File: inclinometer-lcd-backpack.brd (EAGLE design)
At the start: 78.7 x 25.4 mm, 13 parts, among them IC1 ATmega328-DIP-Prgrammed, Q1 2N3904, U1 LCD-16X2NOHOLES, Y1 16MHz

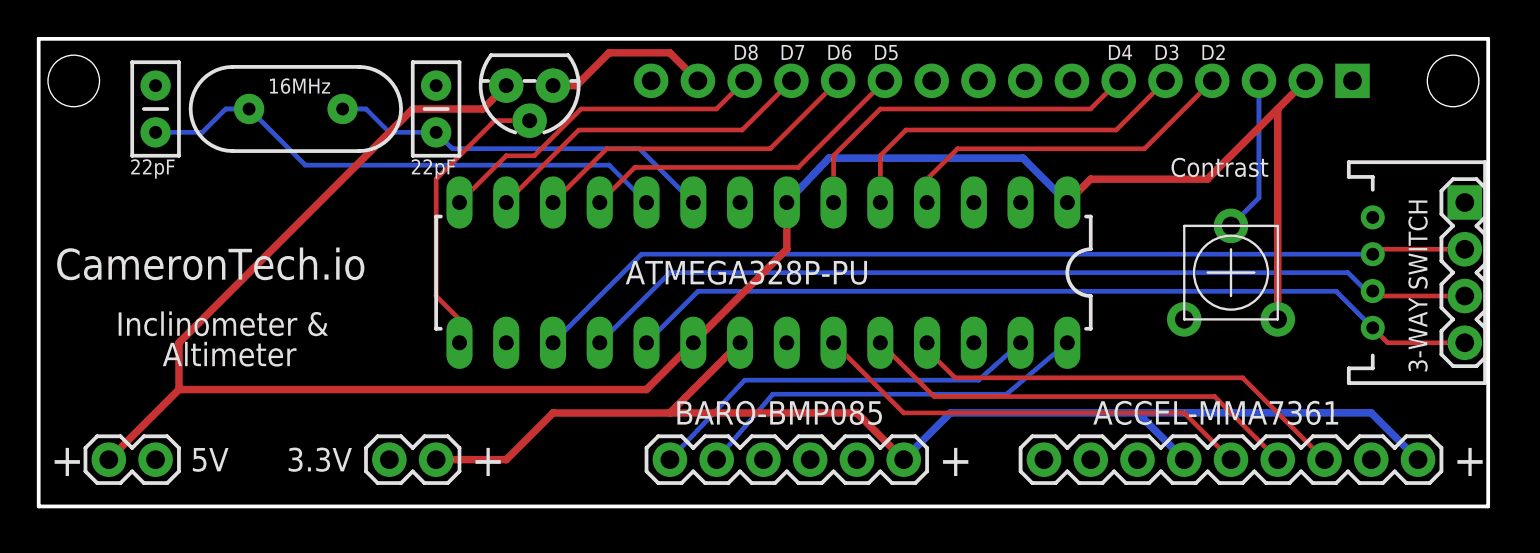
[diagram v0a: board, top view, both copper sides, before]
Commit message: Switches to 10DOF board from Sunkee
http://www.amazon.com/gp/product/B00CD239UG/ref=oh_details_o01_s00_i00?ie=UTF8&psc=1
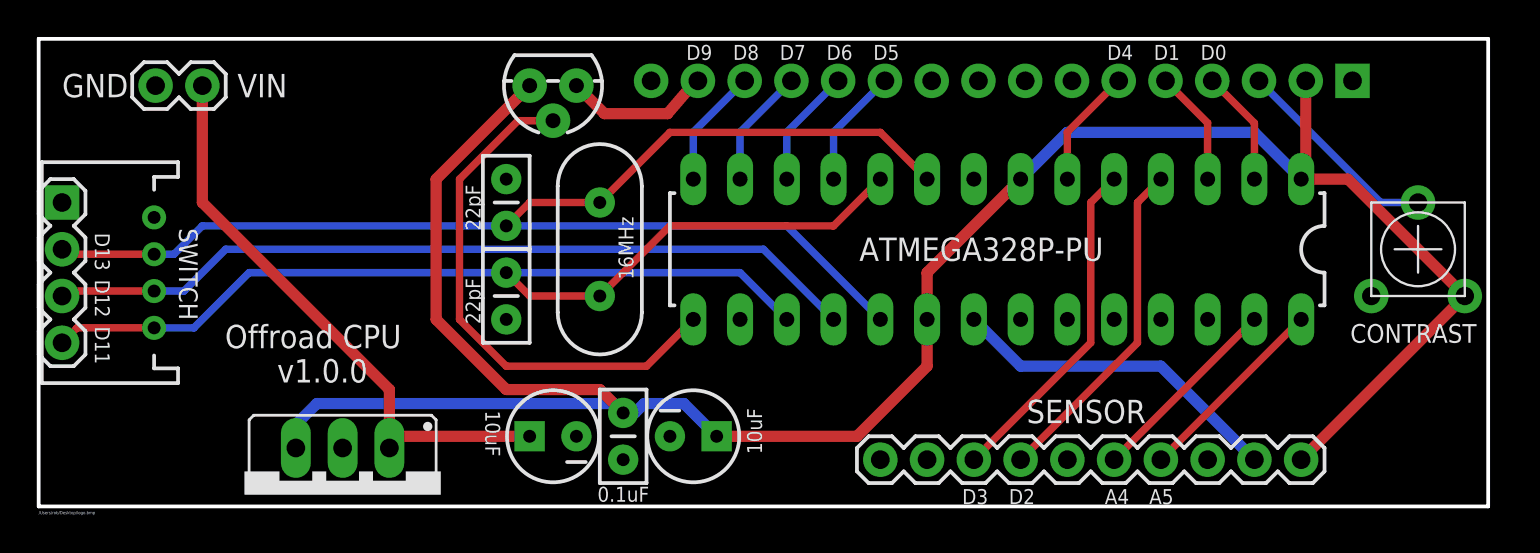
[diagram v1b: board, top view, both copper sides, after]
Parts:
- removed 3.3V, 5V: (no value), SparkFun-Passives:1X02
- removed ACCEL: M09, SparkFun-Connectors:1X09
- removed BARO: (no value), SparkFun:1X06
- added 5VREG: (no value), v-reg:78XXS
- added C3: (no value), SparkFun-Capacitors:CAP-PTH-SMALL2
- added C4, C5: (no value), SparkFun-Capacitors:CPOL-RADIAL-10UF-25V
- added SENSOR: M10", SparkFun-Connectors:1X10
- added VCC: (no value), SparkFun-Passives:1X02
- moved SWITCH 76.2 mm to (1.27, 16.5)
- moved SWITCH-JST 76.2 mm to (1.27, 12.7), turned to 90 degrees
- moved C1 20.5 mm to (25.4, 12.7), turned to 270 degrees
- moved Y1 18.2 mm to (30.5, 14.0), turned to 90 degrees
- moved IC1 12.8 mm to (52.1, 14.0)
- moved R2 10.2 mm to (74.9, 14.0)
- moved C2 6.35 mm to (25.4, 15.2)
- moved Q1 1.27 mm to (27.9, 22.9)
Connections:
- new net INT0: IC1.4, SENSOR.7
- new net INT1: IC1.5, SENSOR.8
- new net VCC: 5VREG.IN, C4.1, VCC.2
- net 3.3V: now also SENSOR.2; no longer 3.3V.2, ACCEL.4, ACCEL.9, BARO.1
- net 5V: now also 5VREG.OUT, C3.1, C5.1, SENSOR.1; no longer 5V.2
- net A0: no longer ACCEL.5
- net A1: no longer ACCEL.6
- net A2: no longer ACCEL.7
- net A4: now also SENSOR.5; no longer BARO.6
- net A5: now also SENSOR.4; no longer BARO.5
- net D11: now also SWITCH-JST.1, SWITCH.4; no longer SWITCH-JST.2, SWITCH.2
- net D12: now also SWITCH-JST.2; no longer SWITCH-JST.3
- net D13: now also SWITCH-JST.3, SWITCH.2; no longer SWITCH-JST.4, SWITCH.4
- net GND: now also 5VREG.GND, C3.2, C4.2, C5.2, SENSOR.3, SWITCH-JST.4, VCC.1; no longer 3.3V.1, 5V.1, ACCEL.8, BARO.2, SWITCH-JST.1
- net R/W: now also IC1.3; no longer IC1.5
- net RS: now also IC1.2; no longer IC1.4
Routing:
- net 3.3V: track 66.5 -> 18.4 mm
- net VCC: track 0.00 -> 31.8 mm
- net A2: track 24.4 -> 0.00 mm
- net A1: track 24.2 -> 0.00 mm
- net A0: track 24.2 -> 0.00 mm
- net INT1: track 0.00 -> 18.4 mm
- net INT0: track 0.00 -> 18.4 mm
- net R/W: track 19.7 -> 6.29 mm
- net E: track 19.7 -> 6.50 mm
- net BL-EN: track 15.8 -> 28.8 mm
- net RS: track 19.0 -> 6.29 mm
- net DB7: track 18.2 -> 6.50 mm
- net DB6: track 18.2 -> 6.50 mm
- net DB5: track 18.2 -> 6.50 mm
- net DB4: track 18.2 -> 6.50 mm
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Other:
- board text added: "/Users/rob/Desktop/logo.bmp"
- board text added: "0.1uF"
- board text added: "10uF"
- board text added: "A4"
- board text added: "A5"
- board text added: "A_INT1"
- board text added: "CONTRAST"
- board text added: "CTORD100"
- board text added: "D0"
- board text added: "D1"
- board text added: "D11"
- board text added: "D12"
- board text added: "D13"
- board text added: "D9"
- board text added: "M_DRDY"
- board text added: "Offroad CPU"
- board text added: "P_EOC"
- board text added: "P_XCLR"
- board text added: "SWITCH"
- board text added: "T_INT1"
- board text added: "VIN"
- board text removed: "+"
- board text removed: "0GD"
- board text removed: "3-WAY SWITCH"
- board text removed: "ACCEL-MMA7361"
- board text removed: "Altimeter"
- board text removed: "BARO-BMP085"
- board text removed: "CTAIM1"
- board text removed: "CameronTech.io"
- board text removed: "Contrast"
- board text removed: "EOC"
- board text removed: "GSEL"
- board text removed: "Inclinometer &"
- board text removed: "SLP"
- board text removed: "ST"
- board text removed: "XCLR"
- board text removed: "XOUT"
- board text removed: "YOUT"
- board text removed: "ZOUT"

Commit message: Adds screw terminals, connects currently unused pins
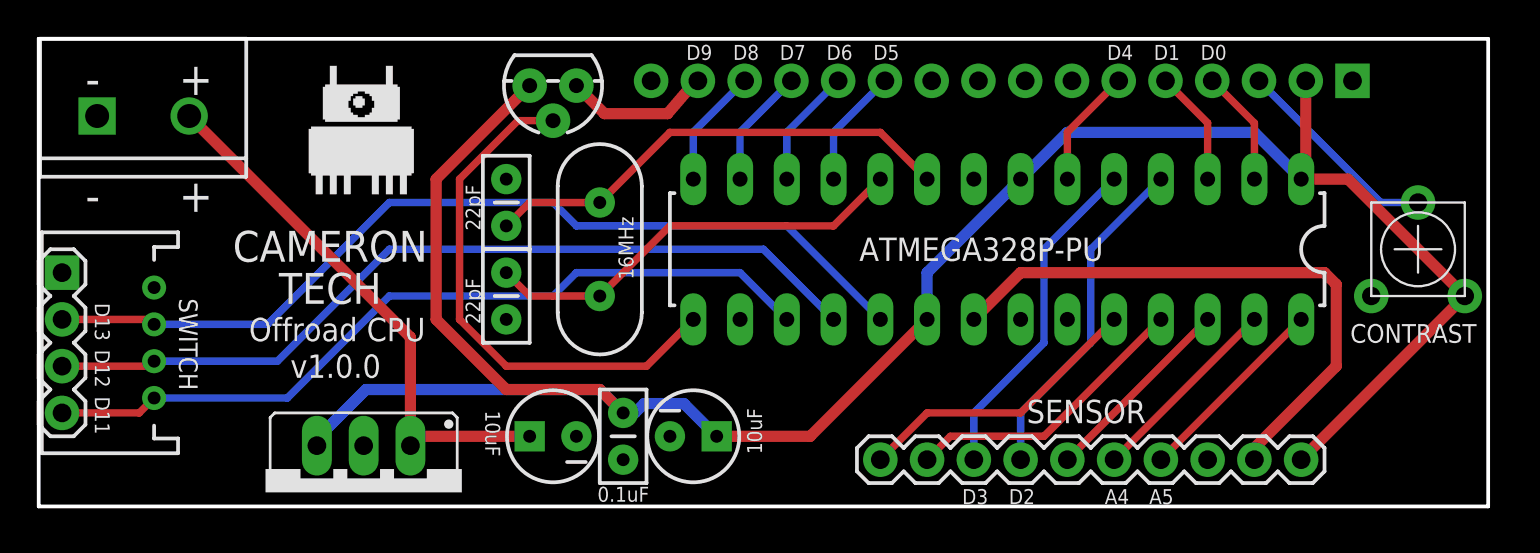
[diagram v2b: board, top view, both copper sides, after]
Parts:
- removed VCC: (no value), SparkFun-Passives:1X02
- added JP1: M025MM, SparkFun-Connectors:SCREWTERMINAL-5MM-2
- moved SWITCH 3.81 mm to (1.27, 12.7)
- moved SWITCH-JST 3.81 mm to (1.27, 8.89)
- moved 5VREG 1.15 mm to (17.7, 0.76)
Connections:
- net A1: now also SENSOR.10
- net A2: now also SENSOR.9
- net A3: now also SENSOR.6
- net GND: now also JP1.1; no longer VCC.1
- net VCC: now also JP1.2; no longer VCC.2
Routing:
- net A1: track 0.00 -> 15.9 mm
- net A2: track 0.00 -> 15.9 mm
- net 3.3V: track 18.4 -> 32.4 mm
- net A3: track 0.00 -> 10.8 mm
- net D13: track 47.3 -> 49.9 mm
- net 5V: track 125.0 -> 122.4 mm
- net VCC: track 31.8 -> 30.0 mm
- net D11: track 42.1 -> 43.6 mm
- net D12: track 44.9 -> 46.1 mm
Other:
- board text added: "+"
- board text added: "-"
- board text added: "CAMERON"
- board text added: "TECH"
- board text removed: "/Users/rob/Desktop/logo.bmp"
- board text removed: "VIN"
